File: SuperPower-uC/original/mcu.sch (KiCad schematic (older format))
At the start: 29 parts, among them J4 mcu_pinout, J5 mcu_pinout, Q5 Q_NPN_CEB, Q6 Q_NPN_CEB, U4 CP2102N-A01-GQFN28, U5 ESP32-WROOM32

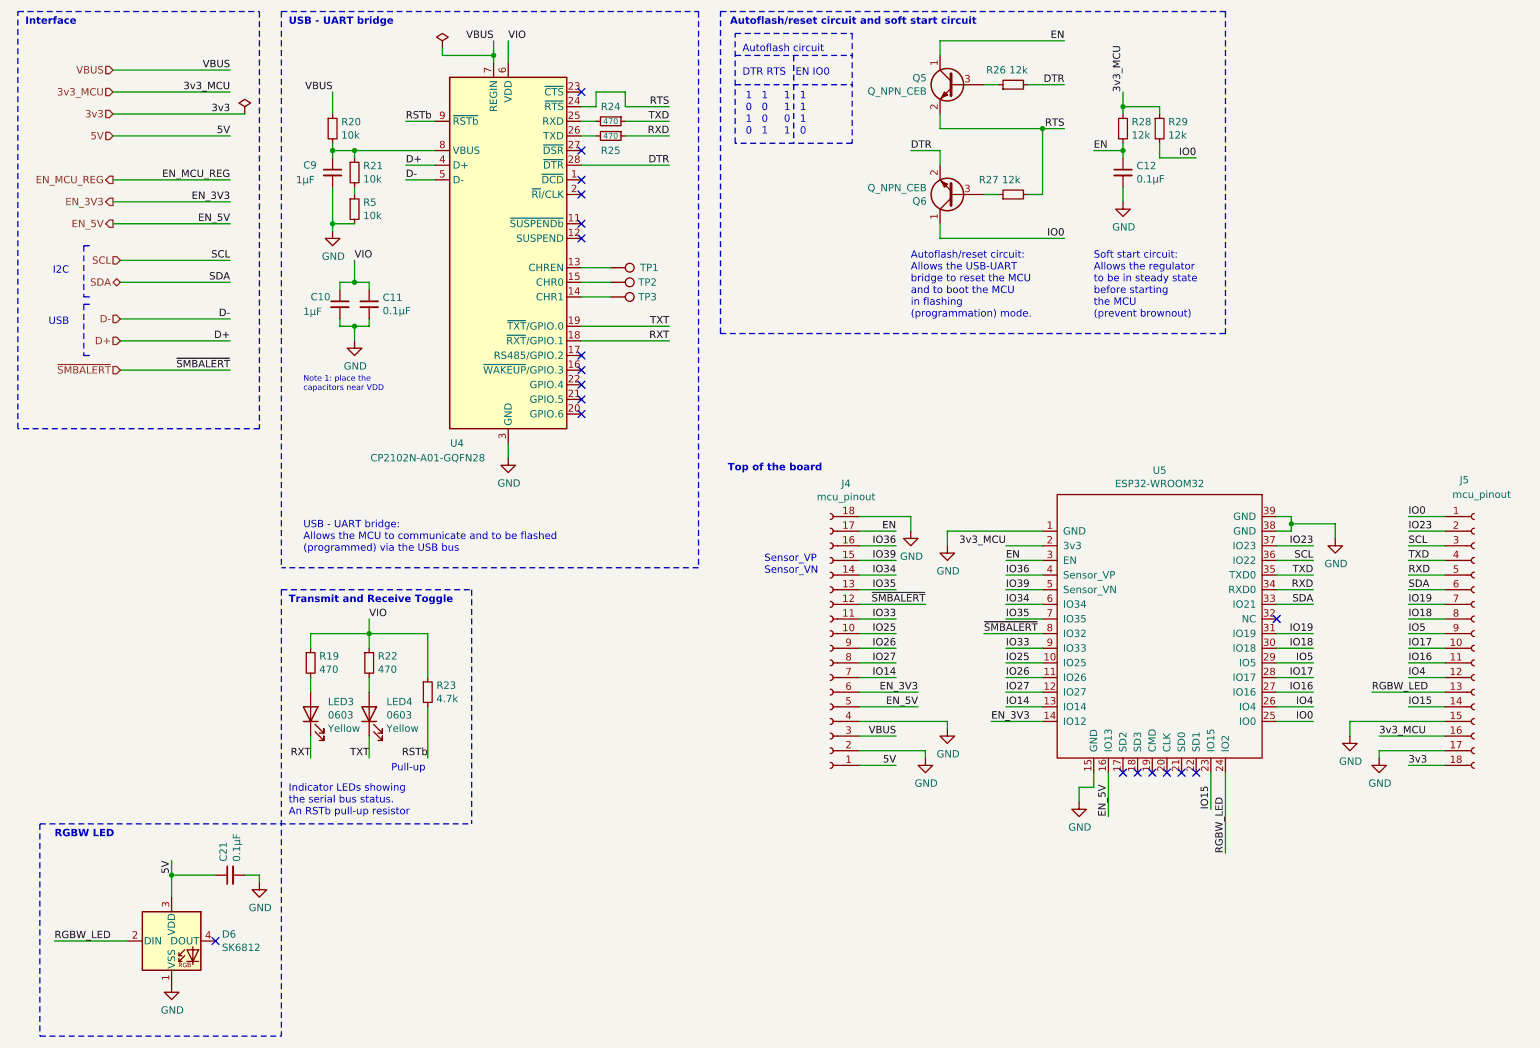
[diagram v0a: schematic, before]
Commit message: Apply some review changes
- add jumper to bypass trc on regulator sheet
- add testpoints on each interface in the MCU sheet
- removed the en_reg track which was not used but added an testpoint just in case
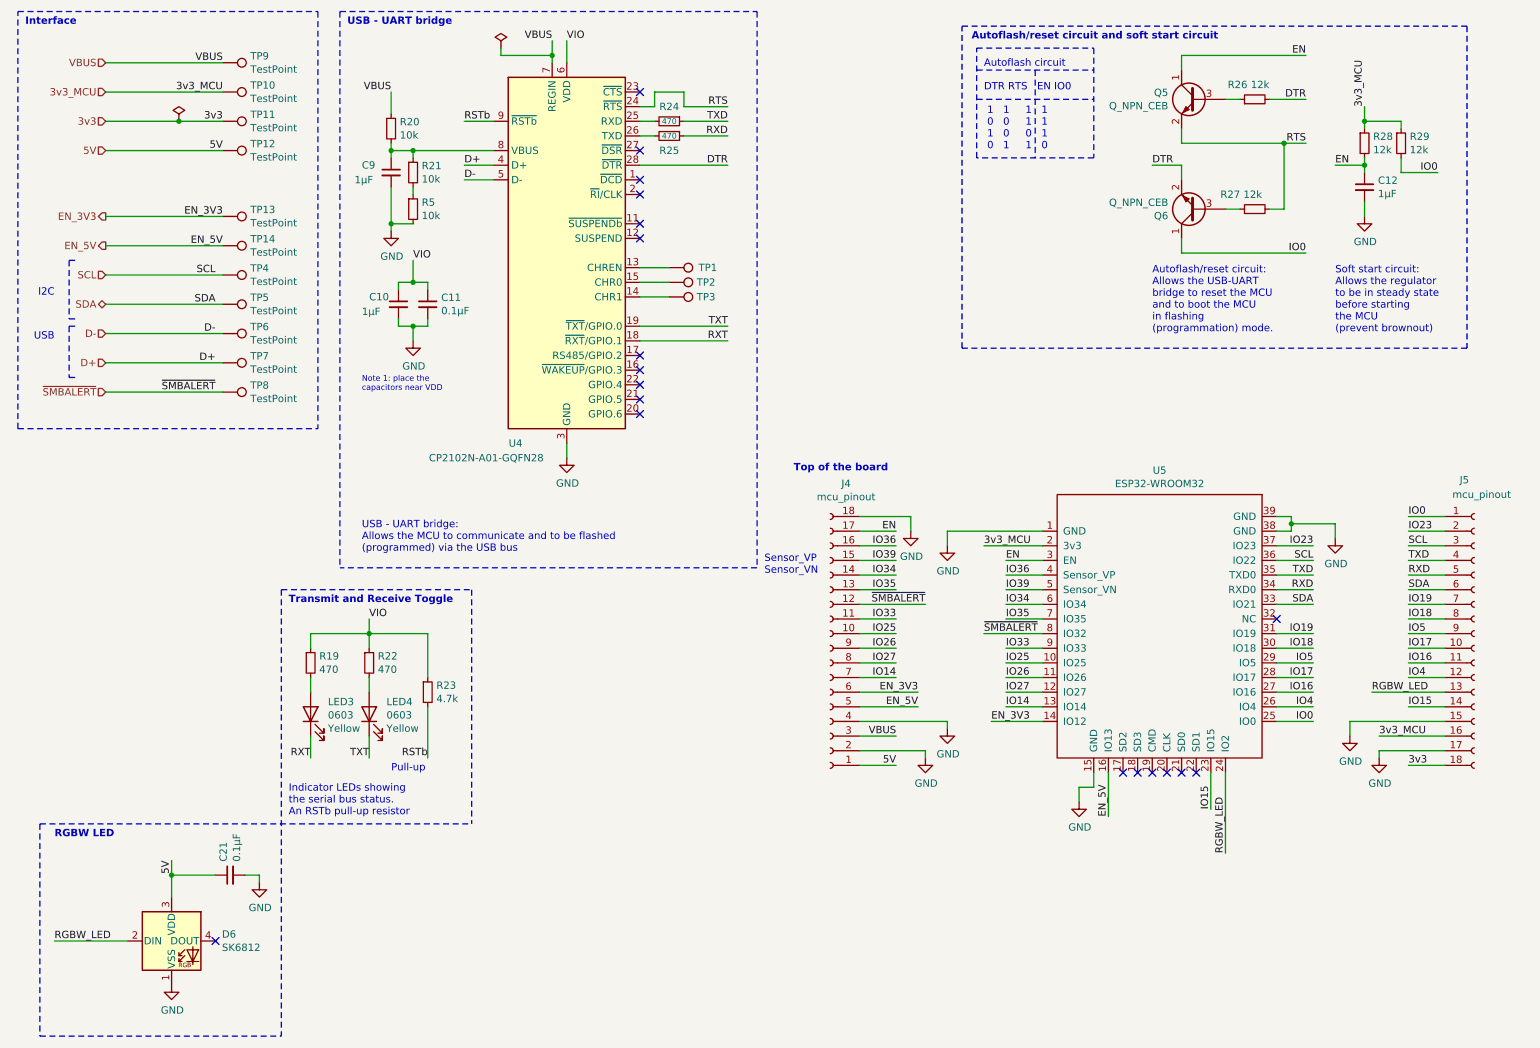
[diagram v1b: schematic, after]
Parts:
- added TP10, TP11, TP12, TP13, TP14, TP4, TP5, TP6, TP7, TP8, TP9: TestPoint, TestPoint:TestPoint_Pad_D1.0mm, symbol Connector:TestPoint
- C12: value 0.1µF -> 1µF
- TP1, TP2, TP3: footprint TestPoint:TestPoint_Pad_D1.5mm -> TestPoint:TestPoint_Pad_D1.0mm
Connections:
- net 3v3: now also TP11.1
- net 3v3_MCU: now also TP10.1
- net 5V: now also TP12.1
- net D+: now also TP7.1
- net D-: now also TP6.1
- net EN_3V3: now also TP13.1
- net EN_5V: now also TP14.1
- net SCL: now also TP4.1
- net SDA: now also TP5.1
- net VBUS: now also TP9.1
- net ~SMBALERT: now also TP8.1
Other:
- moved on the sheet: C10, C11, C12, C9, Q5, Q6, R20, R21, R24, R25, R26, R27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

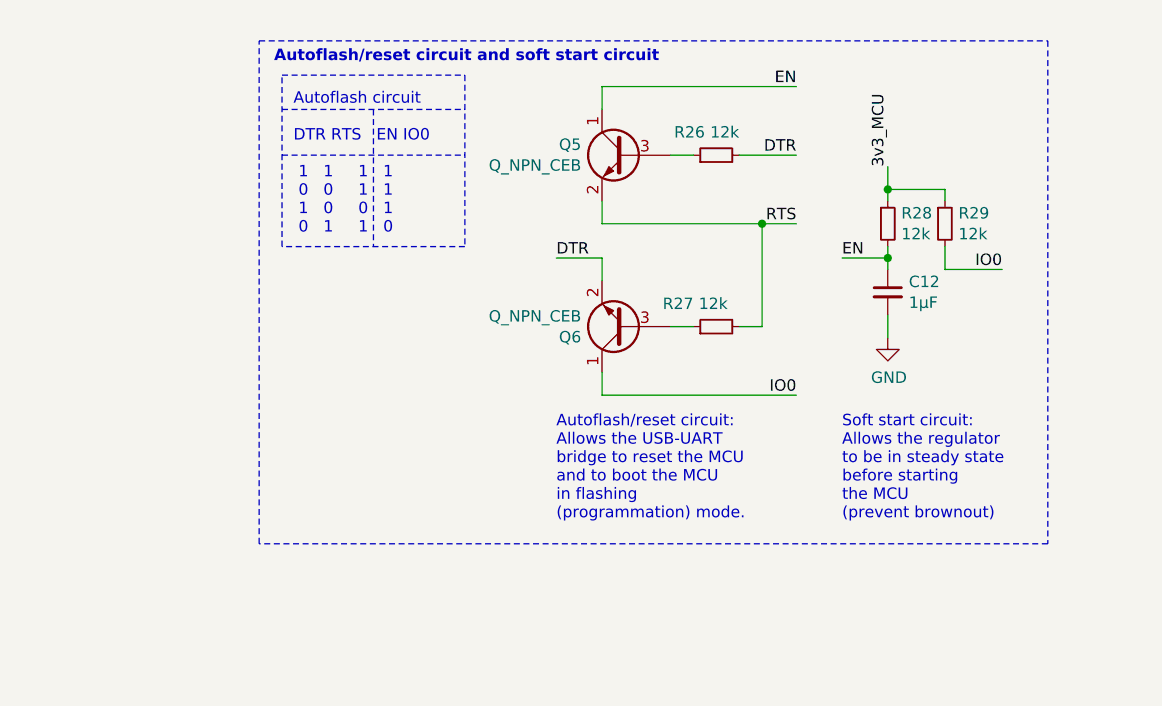
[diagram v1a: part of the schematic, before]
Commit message: Add footprint for auto-reset transistors
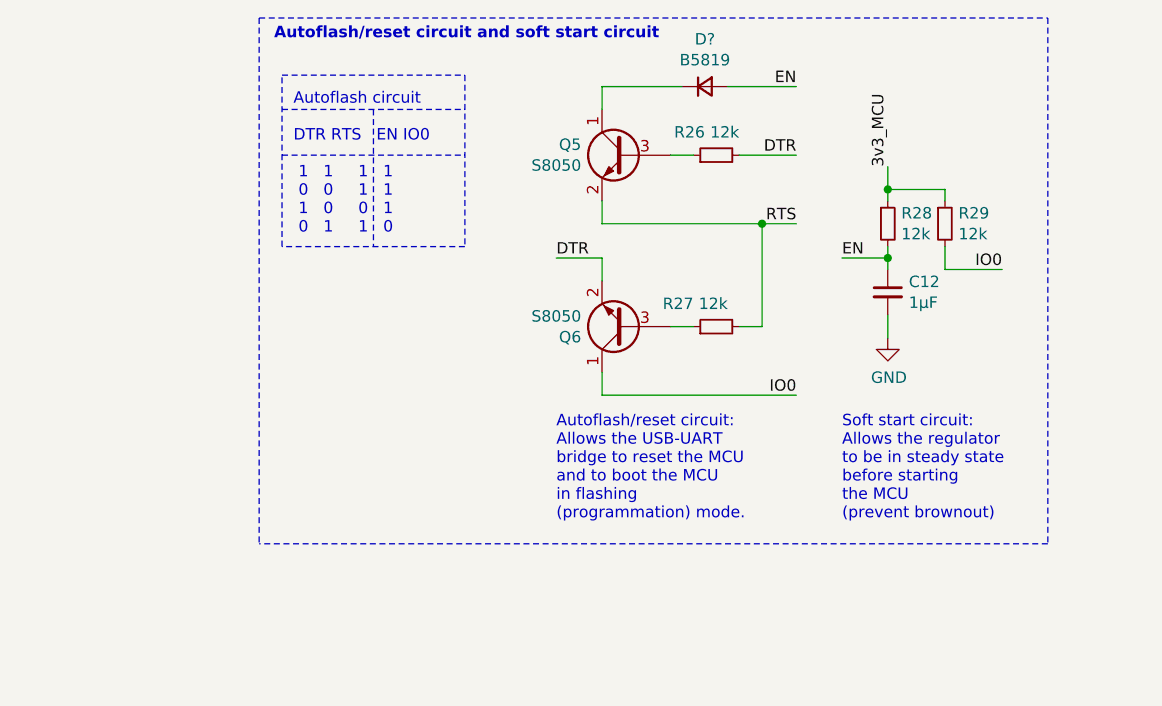
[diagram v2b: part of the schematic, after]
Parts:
- added D?: B5819, symbol Device:D_Small
- Q5, Q6: value Q_NPN_CEB -> S8050; footprint (none) -> Package_TO_SOT_SMD:SOT-23
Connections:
- net EN: now also D?.2 (A); no longer Q5.1 (C)
- new net: D?.1 (K), Q5.1 (C)
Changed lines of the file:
@@
 P 8700 2000
 F 0 "Q6" H 8891 2046 50  0000 L CNN
-F 1 "Q_NPN_CEB" H 8891 1955 50  0000 L CNN
-F 2 "" H 8900 2100 50  0001 C CNN
+F 1 "S8050" H 8891 1955 50  0000 L CNN
+F 2 "Package_TO_SOT_SMD:SOT-23" H 8900 2100 50  0001 C CNN
 F 3 "~" H 8700 2000 50  0001 C CNN
 	1    8700 2000
@@
 Wire Wire Line
 	8600 2200 8600 2300
-Wire Wire Line
-	8600 2300 9450 2300
 Text Label 9450 2300 2    50   ~ 0
 IO0
@@
 Wire Notes Line
 	7600 1050 7600 1650
-Text Notes 8850 850  2    50   ~ 10
+Text Notes 8850 750  2    50   ~ 10
 Autoflash/reset circuit and soft start circuit
 Wire Notes Line
-	7100 750  10550 750
+	7100 650  10550 650
 Wire Notes Line
 	10550 2950 7100 2950
-Wire Notes Line
-	7100 2950 7100 750
-Wire Notes Line
-	10550 750  10550 2950
 Connection ~ 9300 1550
 Wire Notes Line
@@
 	8600 1550 9300 1550
 Wire Wire Line
-	8600 950  9450 950
+	8600 950  8950 950
 Wire Wire Line
 	8600 1050 8600 950
@@
 P 8700 1250
 F 0 "Q5" H 8891 1296 50  0000 L CNN
-F 1 "Q_NPN_CEB" H 8891 1205 50  0000 L CNN
-F 2 "" H 8900 1350 50  0001 C CNN
+F 1 "S8050" H 8891 1205 50  0000 L CNN
+F 2 "Package_TO_SOT_SMD:SOT-23" H 8900 1350 50  0001 C CNN
 F 3 "~" H 8700 1250 50  0001 C CNN
 	1    8700 1250
@@
 	0    1    1    0
 $EndComp
+$Comp
+L Device:D_Small D?
+U 1 1 5FDAA563
+P 9050 950
+F 0 "D?" H 9050 743 50  0000 C CNN
+F 1 "B5819" H 9050 834 50  0000 C CNN
+F 2 "" V 9050 950 50  0001 C CNN
+F 3 "~" V 9050 950 50  0001 C CNN
+	1    9050 950
+	1    0    0    1
+$EndComp
+Wire Wire Line
+	8600 2300 9450 2300
+Wire Wire Line
+	9150 950  9450 950
+Wire Notes Line
+	10550 650  10550 2950
+Wire Notes Line
+	7100 650  7100 2950
 $EndSCHEMATC

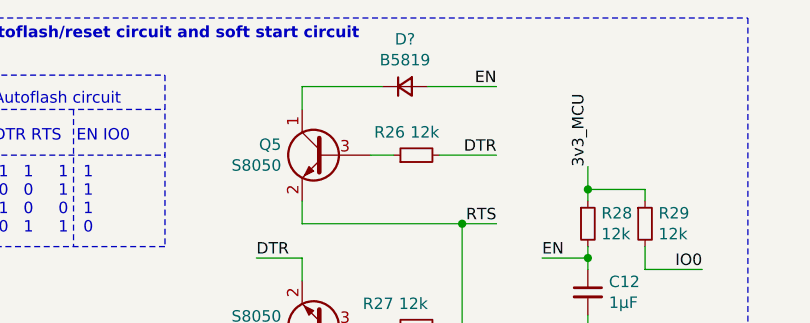
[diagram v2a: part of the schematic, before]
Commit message: Exchanged inductor of the regulators with IHLP2525CZER1R5M01
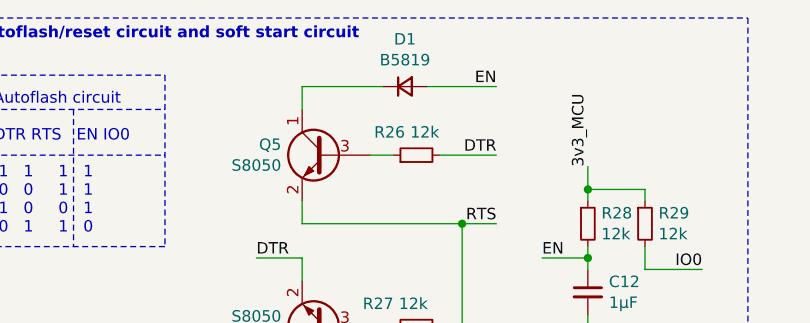
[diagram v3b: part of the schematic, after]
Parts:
- gave numbers to parts that had none: 1
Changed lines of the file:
@@
 $EndComp
 $Comp
-L Device:D_Small D?
+L Device:D_Small D1
 U 1 1 5FDAA563
 P 9050 950
-F 0 "D?" H 9050 743 50  0000 C CNN
+F 0 "D1" H 9050 743 50  0000 C CNN
 F 1 "B5819" H 9050 834 50  0000 C CNN
 F 2 "" V 9050 950 50  0001 C CNN
